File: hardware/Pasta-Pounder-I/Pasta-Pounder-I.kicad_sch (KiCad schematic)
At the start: 57 parts, among them CN1 XT30UPB-M, J1 USB_C_Receptacle, J10 Motor_2-, J11 ESC_VCC, J12 ESC_GND, J4 ESC_Port, J5 JST-SH, J7 Motor_1+, J8 Motor_1-, J9 Motor_2+, Q1 AO3401A, SW1 RESET-SW, SW2 BOOT-SW, SW3 5.8 ZSPT, U1 DRV8874PWPR, U2 DRV8874PWPR, U4 USBLC6-2P6, U5 ESP32S3W1, U7 SY8113BADC

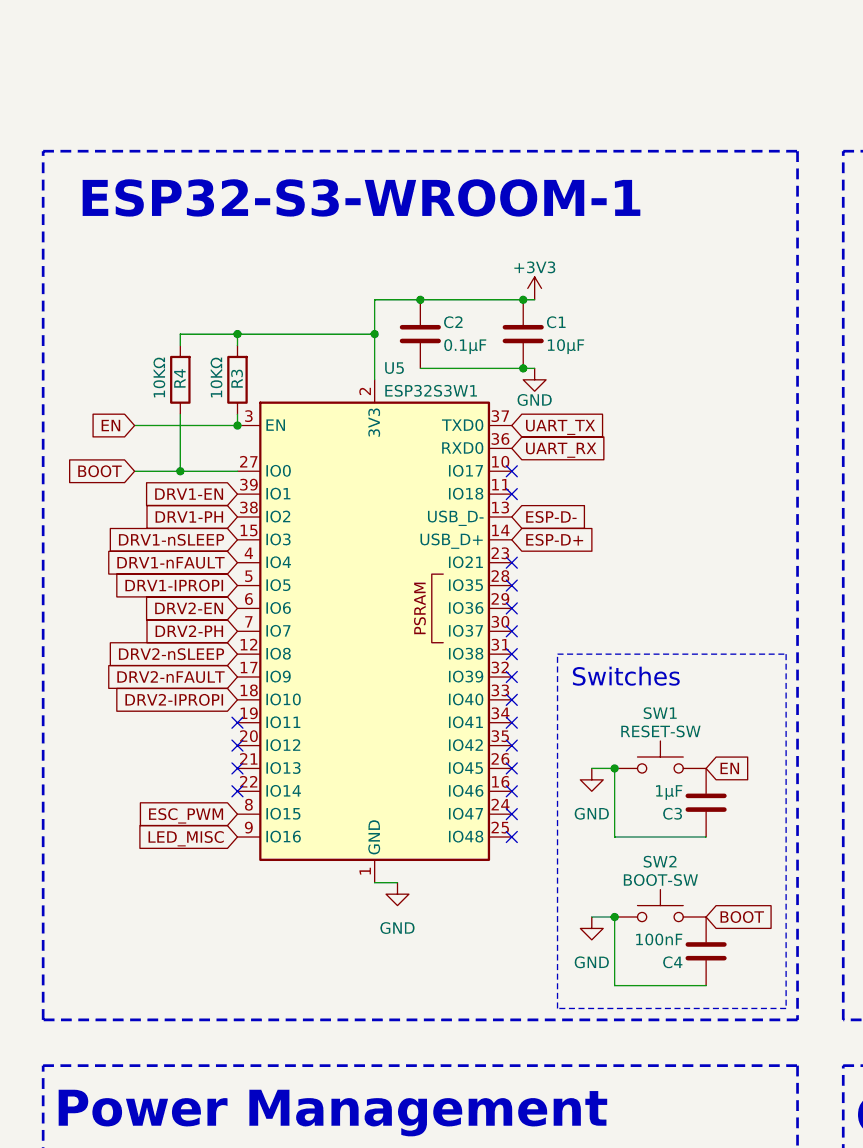
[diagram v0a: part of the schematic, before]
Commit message: Swapped from WROOM-1U to MINI-1U
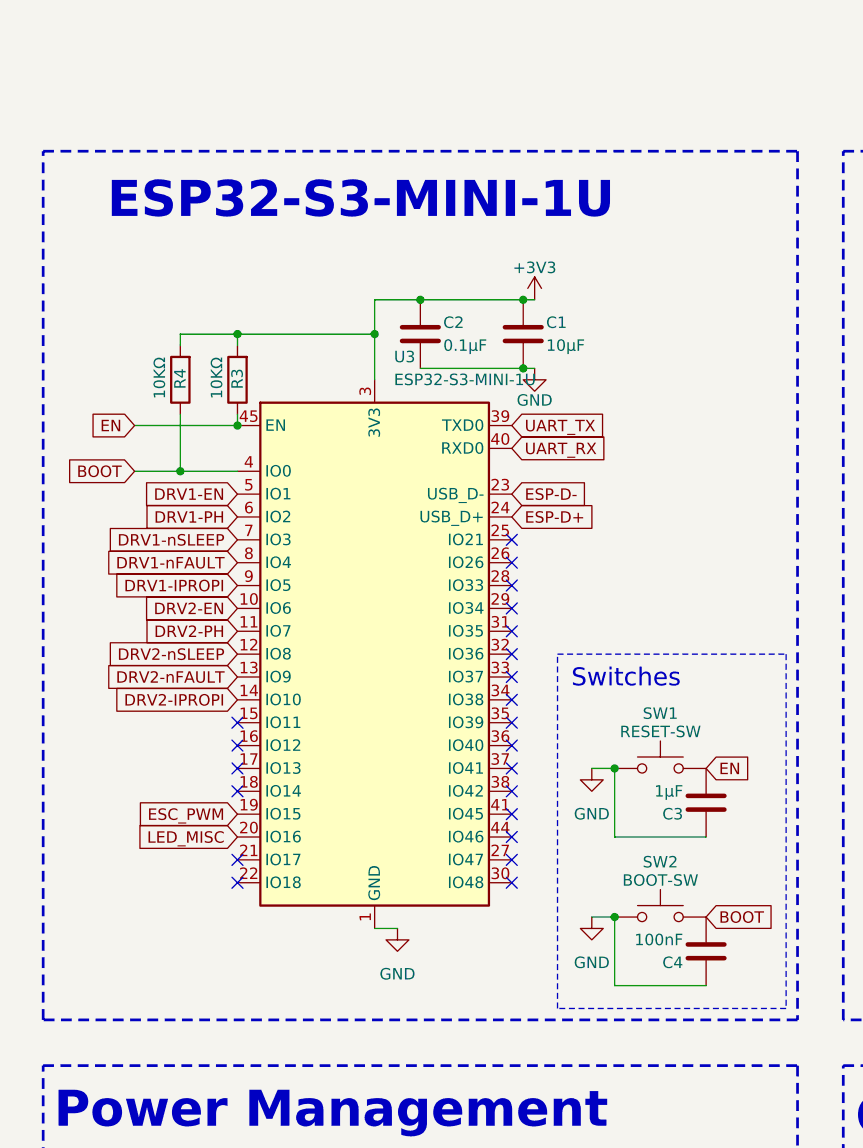
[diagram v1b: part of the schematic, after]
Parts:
- removed U5: ESP32S3W1, lcsc_footprints:C3013946_WIRELM-SMD_ESP32-S3-WROOM-1U, symbol RF_Module:ESP32-S3-WROOM-1
- added U3: ESP32-S3-MINI-1U, RF_Module:ESP32-S2-MINI-1U, symbol RF_Module:ESP32-S3-MINI-1U
- J10, J11, J12, J7, J8, J9: footprint Connector_Wire:SolderWirePad_1x01_SMD_2x4mm -> Connector_Wire:SolderWirePad_1x01_SMD_1x2mm
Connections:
- net +3V3: now also U3.3 (3V3)
- net BOOT: now also U3.4 (IO0)
- net DRV1-EN: now also U3.5 (IO1)
- net DRV1-IPROPI: now also U3.9 (IO5)
- net DRV1-PH: now also U3.6 (IO2)
- net DRV1-nFAULT: now also U3.8 (IO4)
- net DRV1-nSLEEP: now also U3.7 (IO3)
- net DRV2-EN: now also U3.10 (IO6)
- net DRV2-IPROPI: now also U3.14 (IO10)
- net DRV2-PH: now also U3.11 (IO7)
- net DRV2-nFAULT: now also U3.13 (IO9)
- net DRV2-nSLEEP: now also U3.12 (IO8)
- net EN: now also U3.45 (EN)
- net ESC_PWM: now also U3.19 (IO15)
- net ESP-D+: now also U3.24 (USB_D+)
- net ESP-D-: now also U3.23 (USB_D-)
- net GND: now also U3.1 (GND), U3.2 (GND), U3.42 (GND), U3.43 (GND), U3.46 (GND), U3.47 (GND), U3.48 (GND), U3.49 (GND), U3.50 (GND), U3.51 (GND), U3.52 (GND), U3.53 (GND), U3.54 (GND), U3.55 (GND), U3.56 (GND), U3.57 (GND), U3.58 (GND), U3.59 (GND), U3.60 (GND), U3.61 (GND), U3.62 (GND), U3.63 (GND), U3.64 (GND), U3.65 (GND)
- net LED_MISC: now also U3.20 (IO16)
- net UART_RX: now also U3.40 (RXD0)
- net UART_TX: now also U3.39 (TXD0)
- no-connect marks 34 -> 37
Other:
- note added: "ESP32-S3-MINI-1U"
- note removed: "ESP32-S3-WROOM-1"

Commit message: Moved components to fully fit within 70x20mm
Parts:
- C12, C8: footprint Capacitor_SMD:CP_Elec_6.3x7.7 -> PCM_JLCPCB:C_0805
- J10, J11, J12, J7, J8, J9: footprint Connector_Wire:SolderWirePad_1x01_SMD_1x2mm -> Connector_Wire:SolderWirePad_1x01_SMD_2x4mm
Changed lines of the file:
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@@
 			)
 		)
-		(property "Footprint" "Connector_Wire:SolderWirePad_1x01_SMD_1x2mm"
+		(property "Footprint" "Connector_Wire:SolderWirePad_1x01_SMD_2x4mm"
 			(at 154.94 152.4 0)
 			(hide yes)
@@
 			)
 		)
-		(property "Footprint" "Capacitor_SMD:CP_Elec_6.3x7.7"
+		(property "Footprint" "PCM_JLCPCB:C_0805"
 			(at 260.0452 105.41 0)
 			(hide yes)
@@
 			)
 		)
-		(property "Footprint" "Connector_Wire:SolderWirePad_1x01_SMD_1x2mm"
+		(property "Footprint" "Connector_Wire:SolderWirePad_1x01_SMD_2x4mm"
 			(at 124.46 147.32 0)
 			(hide yes)
@@
 			)
 		)
-		(property "Footprint" "Connector_Wire:SolderWirePad_1x01_SMD_1x2mm"
+		(property "Footprint" "Connector_Wire:SolderWirePad_1x01_SMD_2x4mm"
 			(at 124.46 152.4 0)
 			(hide yes)
@@
 			)
 		)
-		(property "Footprint" "Connector_Wire:SolderWirePad_1x01_SMD_1x2mm"
+		(property "Footprint" "Connector_Wire:SolderWirePad_1x01_SMD_2x4mm"
 			(at 154.94 129.54 0)
 			(hide yes)
@@
 			)
 		)
-		(property "Footprint" "Capacitor_SMD:CP_Elec_6.3x7.7"
+		(property "Footprint" "PCM_JLCPCB:C_0805"
 			(at 260.0452 151.13 0)
 			(hide yes)
@@
 			)
 		)
-		(property "Footprint" "Connector_Wire:SolderWirePad_1x01_SMD_1x2mm"
+		(property "Footprint" "Connector_Wire:SolderWirePad_1x01_SMD_2x4mm"
 			(at 154.94 134.62 0)
 			(hide yes)
@@
 			)
 		)
-		(property "Footprint" "Connector_Wire:SolderWirePad_1x01_SMD_1x2mm"
+		(property "Footprint" "Connector_Wire:SolderWirePad_1x01_SMD_2x4mm"
 			(at 154.94 147.32 0)
 			(hide yes)
